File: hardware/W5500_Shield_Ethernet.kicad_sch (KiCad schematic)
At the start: 33 parts, among them J1 HR911105A, J2 Conn_02x05_Odd_Even, U2 W5500, Y1 X322525MOB4SI

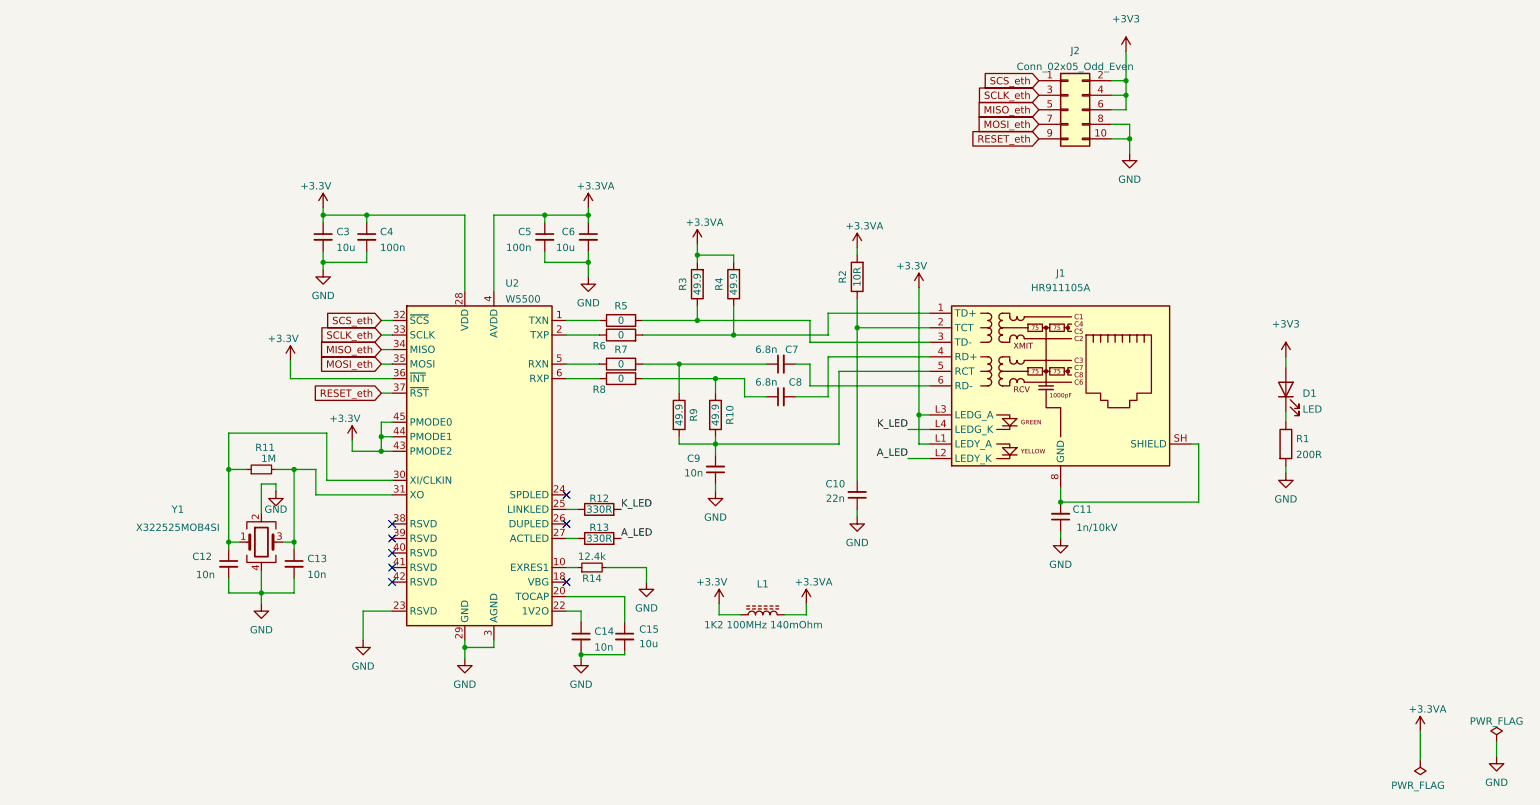
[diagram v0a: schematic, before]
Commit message: added some examples schematic
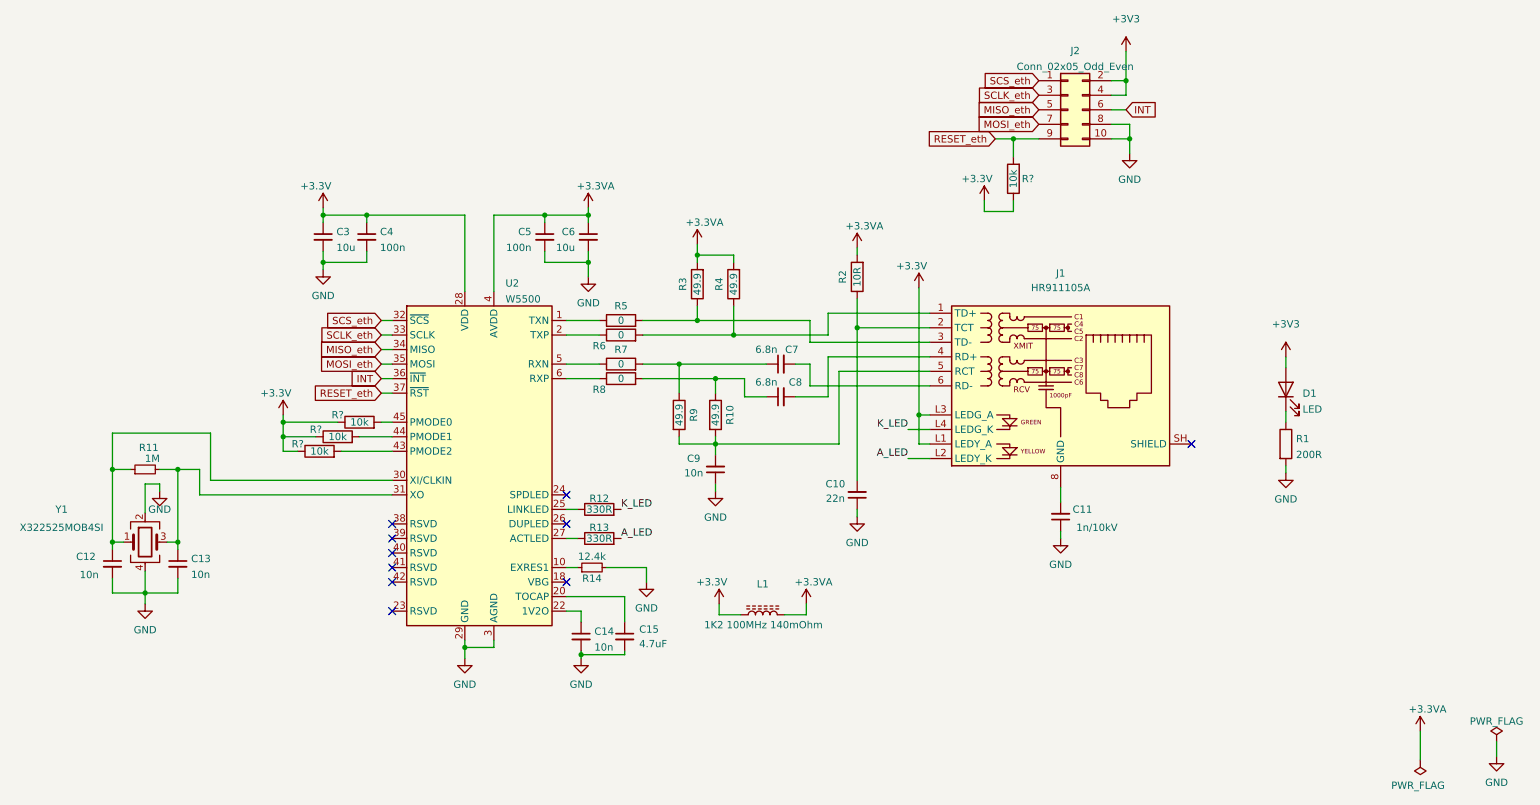
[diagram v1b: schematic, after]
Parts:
- added R? (x4): 10k, Resistor_SMD:R_0402_1005Metric, symbol Device:R
- C15: value 10u -> 4.7uF
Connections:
- net +3V3: now also R?.1, R?.1, R?.1, R?.1; no longer J2.6 (Pin_6), U2.36 (~{INT}), U2.43 (PMODE2), U2.44 (PMODE1), U2.45 (PMODE0)
- net GND: no longer U2.23 (RSVD)
- net RESET_eth: now also R?.2
- net at C11.2, J1.8 (GND): no longer J1.SH (SHIELD)
- new net: R?.2, U2.44 (PMODE1)
- new net: R?.2, U2.43 (PMODE2)
- new net: R?.2, U2.45 (PMODE0)
- new net INT: J2.6 (Pin_6), U2.36 (~{INT})
- no-connect marks 8 -> 10
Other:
- moved on the sheet: C12, C13, R11, Y1
